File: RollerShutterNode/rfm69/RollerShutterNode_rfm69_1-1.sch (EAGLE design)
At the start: 50 parts, among them IC1 ATMega-328, IC2 AT25DF512C-SSHN-B, IC3 MCP1703CB, IC4 ACS712_5A, IC5 ATSHA204A, IC6 LM321, IC7 MDC3105DMT1, X1 8 MHz

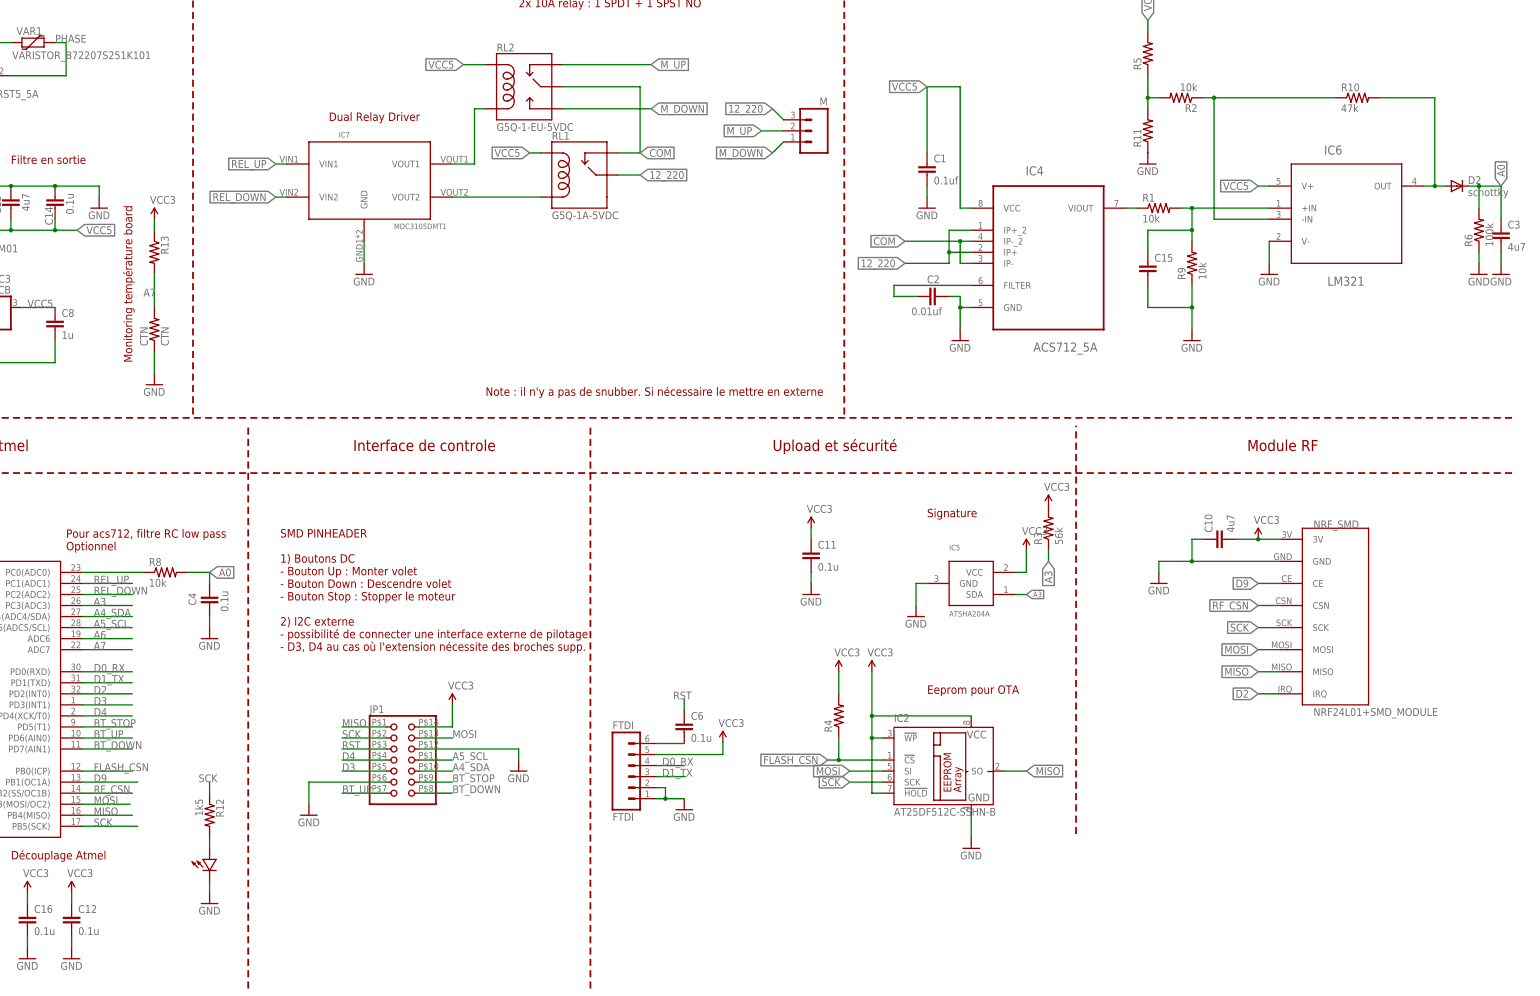
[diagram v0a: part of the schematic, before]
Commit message: 1.1 update
there was a missing mistake I didn't see even if I checked lot of
times...routing derouting mistake...spst relay was always ON. shame on
me!
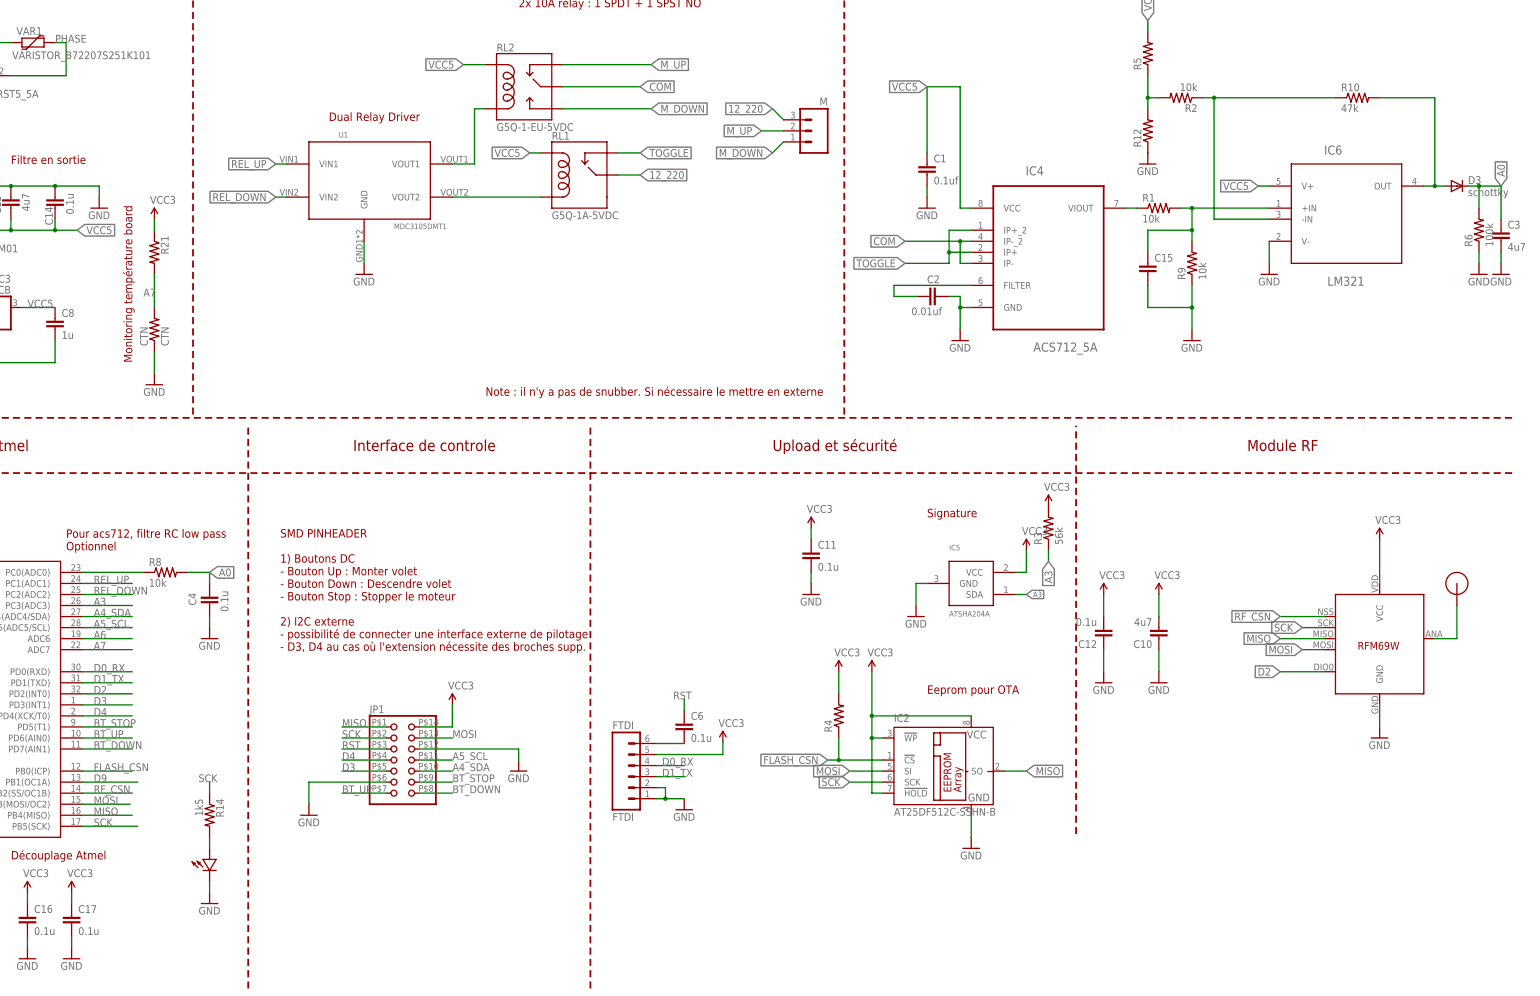
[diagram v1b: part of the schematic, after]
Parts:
- removed NRF_SMD: NRF24L01+SMD_MODULE, pmo_lib:NRF24L01+SMD_MODULE
- removed R11: (no value), LowPowerLab:RESISTOR0805-RES
- added ANT: RFM12B_ANTENNA, LowPowerLab:RFM12B_ANTENNA
- added C17: 0.1u, LowPowerLab:CAP0805-CAP
- added R14: 1k5, LowPowerLab:RESISTOR0805-RES
- added RFM69: RFM69, LowPowerLab:RFM69
- R12: value 1k5 -> (none)
- renumbered D1 to D4, D2 to D3, IC7 to U1, R13 to R21
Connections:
- new net N$4: ANT.1, RFM69.ANT
- new net TOGGLE: IC4.IP+, IC4.IP+_2, RL1.NC
- net 12_220: no longer IC4.IP+, IC4.IP+_2
- net COM: no longer RL1.NC
- net D2: now also RFM69.DIO0; no longer NRF_SMD.IRQ
- net D9: no longer NRF_SMD.CE
- net GND: now also C12.1, C17.2, R12.1, RFM69.GND; no longer C12.2, NRF_SMD.GND, R11.1
- net MISO: now also RFM69.MISO; no longer NRF_SMD.MISO
- net MOSI: now also RFM69.MOSI; no longer NRF_SMD.MOSI
- net N$17: now also R14.2; no longer R12.2
- net N$18: now also R12.2; no longer R11.2
- net RF_CSN: now also RFM69.SEL; no longer NRF_SMD.CSN
- net SCK: now also R14.1, RFM69.SCK; no longer NRF_SMD.SCK, R12.1
- net VCC: now also C12.2, C17.1, RFM69.VCC; no longer C12.1, NRF_SMD.3V
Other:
- moved on the sheet: C10, C12, R12
